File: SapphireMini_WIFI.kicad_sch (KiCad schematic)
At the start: 8 parts, among them M701 AdafruitWINC1500

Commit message: Start of layout
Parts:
- removed L701: 10uH, SapphineMinimal:NR3012T100M, symbol Device:L
- added C601: 22uF, Capacitor_SMD:C_0805_2012Metric, symbol Device:C
- C701: footprint Capacitor_SMD:C_0603_1608Metric -> Capacitor_SMD:C_0805_2012Metric; Voltage (none) -> 16
- C702: footprint Capacitor_SMD:C_0603_1608Metric -> Capacitor_SMD:C_0402_1005Metric; Voltage (none) -> 25
- R701: value 0R25 -> 0; MPN CRCW060347R0FKEAC -> RMCF0603ZT0R00
- R702, R703: MPN (none) -> CRCW060347R0FKEAC
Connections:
- net GND: now also C601.2
- net P3V3: now also C701.1, FB701.1, C601.1
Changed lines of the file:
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@@
   (junction (at 154.94 45.72) (diameter 0) (color 0 0 0 0)
+  )
+  (junction (at 114.3 45.72) (diameter 0) (color 0 0 0 0)
   )
   (junction (at 149.86 45.72) (diameter 0) (color 0 0 0 0)
@@
     (stroke (width 0) (type default) (color 0 0 0 0))
   )
+  (wire (pts (xy 114.3 53.34) (xy 114.3 54.61))
+    (stroke (width 0) (type default) (color 0 0 0 0))
+  )
   (wire (pts (xy 160.02 45.72) (xy 154.94 45.72))
     (stroke (width 0) (type default) (color 0 0 0 0))
   )
+  (wire (pts (xy 114.3 45.72) (xy 125.73 45.72))
+    (stroke (width 0) (type default) (color 0 0 0 0))
+  )
   (wire (pts (xy 158.75 54.61) (xy 157.48 53.34))
     (stroke (width 0) (type default) (color 0 0 0 0))
   )
-  (wire (pts (xy 111.76 45.72) (xy 101.6 45.72))
-    (stroke (width 0) (type default) (color 0 0 0 0))
-  )
   (wire (pts (xy 151.13 76.2) (xy 134.62 76.2))
     (stroke (width 0) (type default) (color 0 0 0 0))
@@
     (stroke (width 0) (type default) (color 0 0 0 0))
   )
-  (wire (pts (xy 125.73 45.72) (xy 119.38 45.72))
+  (wire (pts (xy 101.6 45.72) (xy 114.3 45.72))
     (stroke (width 0) (type default) (color 0 0 0 0))
   )
@@
     (property "Reference" "C702" (id 0) (at 146.05 46.99 0))
     (property "Value" "100nF" (id 1) (at 146.05 52.07 0))
-    (property "Footprint" "Capacitor_SMD:C_0603_1608Metric" (id 2) (at 150.8252 53.34 0)
+    (property "Footprint" "Capacitor_SMD:C_0402_1005Metric" (id 2) (at 150.8252 53.34 0)
       (effects (font (size 1.27 1.27)) hide)
     )
@@
     )
     (property "Populate" "1" (id 7) (at 149.86 49.53 0)
+      (effects (font (size 1.27 1.27)) hide)
+    )
+    (property "Voltage" "25" (id 8) (at 149.86 49.53 0)
       (effects (font (size 1.27 1.27)) hide)
     )
@@
     (property "Reference" "C701" (id 0) (at 121.92 46.99 0))
     (property "Value" "22uF" (id 1) (at 123.19 52.07 0))
-    (property "Footprint" "Capacitor_SMD:C_0603_1608Metric" (id 2) (at 126.6952 53.34 0)
+    (property "Footprint" "Capacitor_SMD:C_0805_2012Metric" (id 2) (at 126.6952 53.34 0)
       (effects (font (size 1.27 1.27)) hide)
     )
@@
     )
     (property "Populate" "1" (id 7) (at 125.73 49.53 0)
+      (effects (font (size 1.27 1.27)) hide)
+    )
+    (property "Voltage" "16" (id 8) (at 125.73 49.53 0)
       (effects (font (size 1.27 1.27)) hide)
     )
@@
     (in_bom yes) (on_board yes)
     (property "Reference" "R701" (id 0) (at 140.97 40.64 90))
-    (property "Value" "0R25" (id 1) (at 140.97 43.18 90))
+    (property "Value" "0" (id 1) (at 140.97 43.18 90))
     (property "Footprint" "Resistor_SMD:R_0603_1608Metric" (id 2) (at 140.97 45.72 0)
       (effects (font (size 1.27 1.27)) hide)
@@
       (effects (font (size 1.27 1.27)) hide)
     )
-    (property "MPN" "CRCW060347R0FKEAC" (id 7) (at 140.97 45.72 0)
+    (property "MPN" "RMCF0603ZT0R00" (id 7) (at 140.97 45.72 0)
       (effects (font (size 1.27 1.27)) hide)
     )
@@
       (effects (font (size 1.27 1.27)) hide)
     )
-    (property "Description" "47 Ohms ±1% 0.1W, 1/10W Chip Resistor 0603" (id 13) (at 140.97 45.72 0)
+    (property "Description" "0 Ohms Jumper 0.1W, 1/10W Chip Resistor 0603 (1608 Metric) Automotive AEC-Q200 Thick Film" (id 13) (at 140.97 45.72 0)
       (effects (font (size 1.27 1.27)) hide)
     )
@@
       (effects (font (size 1.27 1.27)) hide)
     )
+    (property "Description" "47 Ohms ±1% 0.1W, 1/10W Chip Resistor 0603" (id 4) (at 154.94 76.2 0)
+      (effects (font (size 1.27 1.27)) hide)
+    )
+    (property "MPN" "CRCW060347R0FKEAC" (id 5) (at 154.94 76.2 0)
+      (effects (font (size 1.27 1.27)) hide)
+    )
     (pin "1")
     (pin "2")
@@
     )
     (property "Datasheet" "~" (id 3) (at 154.94 71.12 0)
+      (effects (font (size 1.27 1.27)) hide)
+    )
+    (property "Description" "47 Ohms ±1% 0.1W, 1/10W Chip Resistor 0603" (id 4) (at 154.94 71.12 0)
+      (effects (font (size 1.27 1.27)) hide)
+    )
+    (property "MPN" "CRCW060347R0FKEAC" (id 5) (at 154.94 71.12 0)
+      (effects (font (size 1.27 1.27)) hide)
+    )
+    (pin "1")
+    (pin "2")
+  )
+  (symbol (lib_id "power:GND") (at 114.3 54.61 0) (unit 1)
+    (in_bom yes) (on_board yes)
+    (property "Reference" "#PWR0108" (id 0) (at 114.3 60.96 0)
+      (effects (font (size 1.27 1.27)) hide)
+    )
+    (property "Value" "GND" (id 1) (at 114.427 59.0042 0))
+    (property "Footprint" "" (id 2) (at 114.3 54.61 0)
+      (effects (font (size 1.27 1.27)) hide)
+    )
+    (property "Datasheet" "" (id 3) (at 114.3 54.61 0)
+      (effects (font (size 1.27 1.27)) hide)
+    )
+    (pin "1")
+  )
+  (symbol (lib_id "Device:C") (at 114.3 49.53 0) (unit 1)
+    (in_bom yes) (on_board yes)
+    (property "Reference" "C601" (id 0) (at 110.49 46.99 0))
+    (property "Value" "22uF" (id 1) (at 111.76 52.07 0))
+    (property "Footprint" "Capacitor_SMD:C_0805_2012Metric" (id 2) (at 115.2652 53.34 0)
+      (effects (font (size 1.27 1.27)) hide)
+    )
+    (property "Datasheet" "~" (id 3) (at 114.3 49.53 0)
+      (effects (font (size 1.27 1.27)) hide)
+    )
+    (property "Description" "22 µF ±20% 25V Ceramic Capacitor X5R 0805 (2012 Metric)" (id 4) (at 114.3 49.53 0)
+      (effects (font (size 1.27 1.27)) hide)
+    )
+    (property "MPN" "CL21A226MAYNNNE" (id 5) (at 114.3 49.53 0)
+      (effects (font (size 1.27 1.27)) hide)
+    )
+    (property "Manufacturer" "Samsung" (id 6) (at 114.3 49.53 0)
+      (effects (font (size 1.27 1.27)) hide)
+    )
+    (property "Populate" "1" (id 7) (at 114.3 49.53 0)
+      (effects (font (size 1.27 1.27)) hide)
+    )
+    (property "Voltage" "16" (id 8) (at 114.3 49.53 0)
       (effects (font (size 1.27 1.27)) hide)
     )
@@
       (effects (font (size 1.27 1.27)) hide)
     )
-    (pin "1")
-    (pin "2")
-  )
-  (symbol (lib_id "Device:L") (at 115.57 45.72 90) (unit 1)
-    (in_bom yes) (on_board yes)
-    (property "Reference" "L701" (id 0) (at 114.3 44.45 90)
-      (effects (font (size 1.27 1.27)) (justify left))
-    )
-    (property "Value" "10uH" (id 1) (at 120.65 44.45 90)
-      (effects (font (size 1.27 1.27)) (justify left))
-    )
-    (property "Footprint" "SapphineMinimal:NR3012T100M" (id 2) (at 115.57 45.72 0)
-      (effects (font (size 1.27 1.27)) hide)
-    )
-    (property "Datasheet" "~" (id 3) (at 115.57 45.72 0)
-      (effects (font (size 1.27 1.27)) hide)
-    )
-    (property "Description" "FIXED IND 10UH 630MA 348MOHM SMD" (id 4) (at 115.57 45.72 0)
-      (effects (font (size 1.27 1.27)) hide)
-    )
-    (property "MPN" "NR3012T100M" (id 5) (at 115.57 45.72 0)
-      (effects (font (size 1.27 1.27)) hide)
-    )
-    (property "Manufacturer" "Taiyo Yuden" (id 6) (at 115.57 45.72 0)
-      (effects (font (size 1.27 1.27)) hide)
-    )

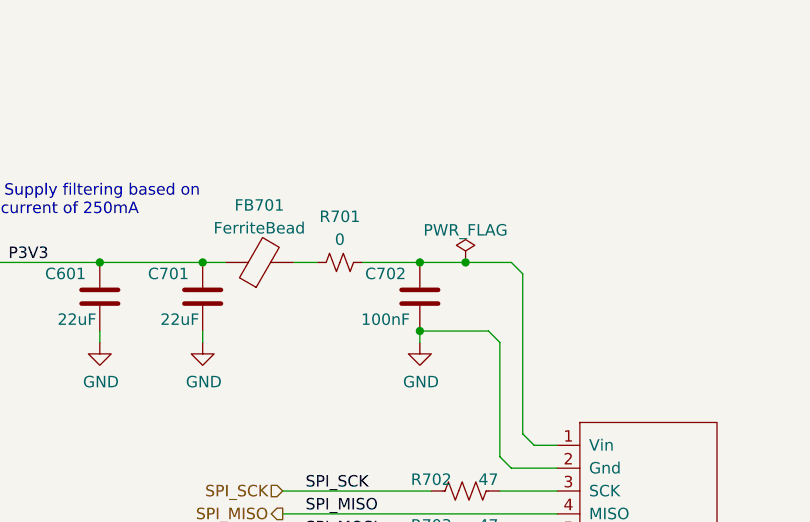
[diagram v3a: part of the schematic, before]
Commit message: updated new layout - no routing
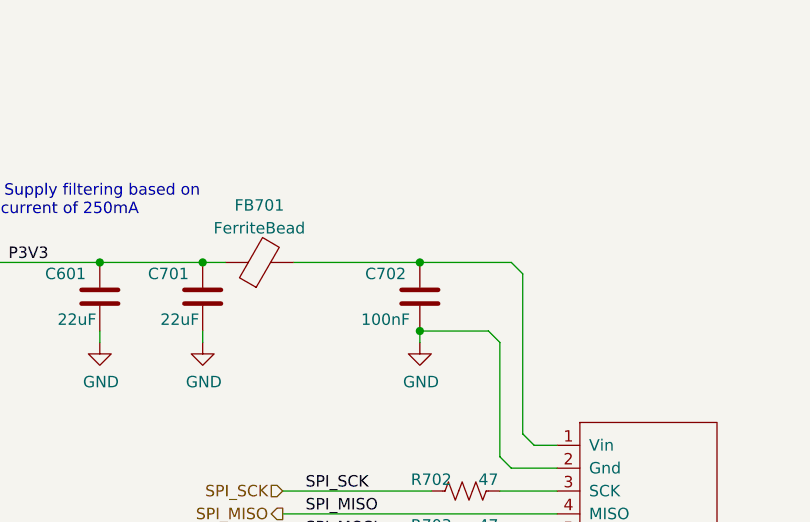
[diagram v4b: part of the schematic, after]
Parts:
- removed R701: 0, Resistor_SMD:R_0603_1608Metric, symbol Device:R_Small_US
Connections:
- net at C702.1, M701.1 (Vin): now also FB701.2
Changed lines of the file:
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@@
     (comment 2 "Markup copy w/ errors!")
-  )
-  (junction (at 154.94 45.72) (diameter 0) (color 0 0 0 0)
   )
   (junction (at 114.3 45.72) (diameter 0) (color 0 0 0 0)
@@
     (stroke (width 0) (type default) (color 0 0 0 0))
   )
+  (wire (pts (xy 135.89 45.72) (xy 149.86 45.72))
+    (stroke (width 0) (type default) (color 0 0 0 0))
+  )
   (wire (pts (xy 162.56 66.04) (xy 161.29 64.77))
     (stroke (width 0) (type default) (color 0 0 0 0))
@@
     (stroke (width 0) (type default) (color 0 0 0 0))
   )
-  (wire (pts (xy 135.89 45.72) (xy 138.43 45.72))
-    (stroke (width 0) (type default) (color 0 0 0 0))
-  )
-  (wire (pts (xy 154.94 45.72) (xy 149.86 45.72))
+  (wire (pts (xy 149.86 45.72) (xy 160.02 45.72))
     (stroke (width 0) (type default) (color 0 0 0 0))
   )
@@
     (stroke (width 0) (type default) (color 0 0 0 0))
   )
-  (wire (pts (xy 160.02 45.72) (xy 154.94 45.72))
-    (stroke (width 0) (type default) (color 0 0 0 0))
-  )
   (wire (pts (xy 114.3 45.72) (xy 125.73 45.72))
     (stroke (width 0) (type default) (color 0 0 0 0))
@@
   )
   (wire (pts (xy 165.1 78.74) (xy 134.62 78.74))
-    (stroke (width 0) (type default) (color 0 0 0 0))
-  )
-  (wire (pts (xy 143.51 45.72) (xy 149.86 45.72))
     (stroke (width 0) (type default) (color 0 0 0 0))
   )
@@
     (pin "1")
   )
-  (symbol (lib_id "Device:R_Small_US") (at 140.97 45.72 90) (unit 1)
-    (in_bom yes) (on_board yes)
-    (property "Reference" "R701" (id 0) (at 140.97 40.64 90))
-    (property "Value" "0" (id 1) (at 140.97 43.18 90))
-    (property "Footprint" "Resistor_SMD:R_0603_1608Metric" (id 2) (at 140.97 45.72 0)
-      (effects (font (size 1.27 1.27)) hide)
-    )
-    (property "Datasheet" "~" (id 3) (at 140.97 45.72 0)
-      (effects (font (size 1.27 1.27)) hide)
-    )
-    (property "DigiKey Price" "0.05" (id 4) (at 140.97 45.72 0)
-      (effects (font (size 1.27 1.27)) hide)
-    )
-    (property "Manufacturer" "Vishay" (id 5) (at 140.97 45.72 0)
-      (effects (font (size 1.27 1.27)) hide)
-    )
-    (property "Tolerance" "5%" (id 6) (at 140.97 45.72 0)
-      (effects (font (size 1.27 1.27)) hide)
-    )
-    (property "MPN" "RMCF0603ZT0R00" (id 7) (at 140.97 45.72 0)
-      (effects (font (size 1.27 1.27)) hide)
-    )
-    (property "Populate" "1" (id 8) (at 140.97 45.72 0)
-      (effects (font (size 1.27 1.27)) hide)
-    )
-    (property "MacroFab_PN" "MF-RES-0603-47" (id 9) (at 140.97 45.72 0)
-      (effects (font (size 1.27 1.27)) hide)
-    )
-    (property "Digi-Key_PN" "541-5440-1-ND" (id 10) (at 140.97 45.72 0)
-      (effects (font (size 1.27 1.27)) hide)
-    )
-    (property "Distributor" "Digikey" (id 11) (at 140.97 45.72 0)
-      (effects (font (size 1.27 1.27)) hide)
-    )
-    (property "DPN" "541-5440-1-ND" (id 12) (at 140.97 45.72 0)
-      (effects (font (size 1.27 1.27)) hide)
-    )
-    (property "Description" "0 Ohms Jumper 0.1W, 1/10W Chip Resistor 0603 (1608 Metric) Automotive AEC-Q200 Thick Film" (id 13) (at 140.97 45.72 0)
-      (effects (font (size 1.27 1.27)) hide)
-    )
-    (pin "1")
-    (pin "2")
-  )
   (symbol (lib_id "Device:R_US") (at 154.94 76.2 270) (unit 1)
     (in_bom yes) (on_board yes)
@@
     (pin "2")
   )
-  (symbol (lib_id "power:PWR_FLAG") (at 154.94 45.72 0) (unit 1)
-    (in_bom yes) (on_board yes) (fields_autoplaced)
-    (property "Reference" "#FLG0701" (id 0) (at 154.94 43.815 0)
-      (effects (font (size 1.27 1.27)) hide)
-    )
-    (property "Value" "PWR_FLAG" (id 1) (at 154.94 42.1442 0))
-    (property "Footprint" "" (id 2) (at 154.94 45.72 0)
-      (effects (font (size 1.27 1.27)) hide)
-    )
-    (property "Datasheet" "~" (id 3) (at 154.94 45.72 0)
-      (effects (font (size 1.27 1.27)) hide)
-    )
-    (pin "1")
-  )
 )

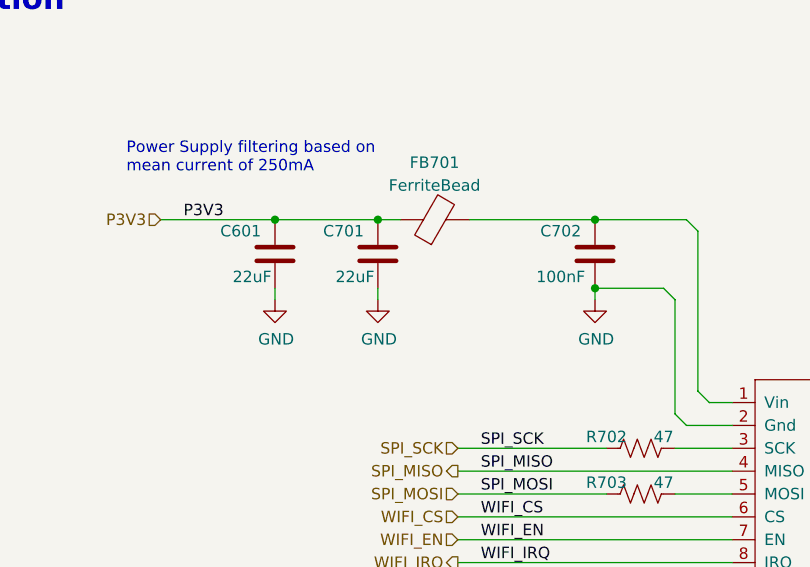
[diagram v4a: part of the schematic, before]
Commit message: 6 Layer Routing
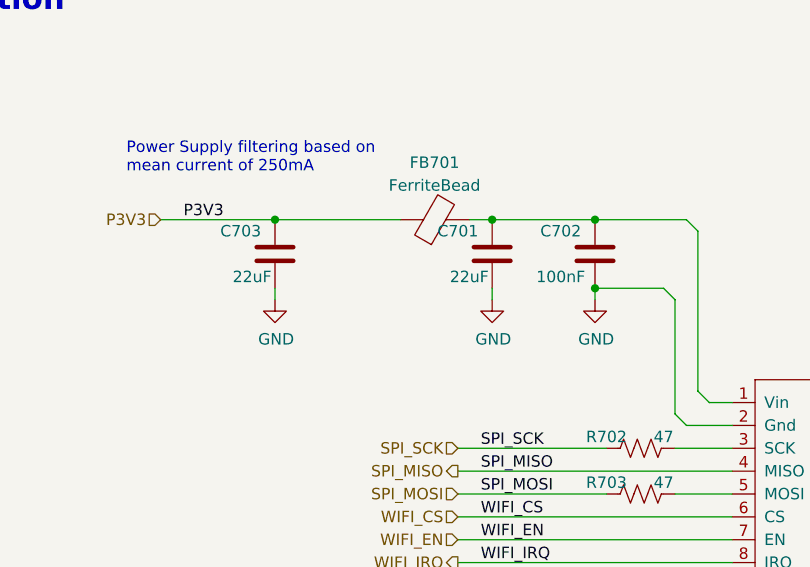
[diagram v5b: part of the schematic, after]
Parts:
- FB701: footprint Inductor_SMD:L_0201_0603Metric -> Inductor_SMD:L_0603_1608Metric
- renumbered C601 to C703
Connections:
- net P3V3: no longer C701.1
- net at C702.1, FB701.2, M701.1 (Vin): now also C701.1
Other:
- moved on the sheet: C701
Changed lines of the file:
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@@
     (comment 2 "Markup copy w/ errors!")
   )
+  (junction (at 138.43 45.72) (diameter 0) (color 0 0 0 0)
+  )
   (junction (at 114.3 45.72) (diameter 0) (color 0 0 0 0)
   )
   (junction (at 149.86 45.72) (diameter 0) (color 0 0 0 0)
-  )
-  (junction (at 125.73 45.72) (diameter 0) (color 0 0 0 0)
   )
   (junction (at 149.86 53.34) (diameter 0) (color 0 0 0 0)
@@
     (stroke (width 0) (type default) (color 0 0 0 0))
   )
-  (wire (pts (xy 135.89 45.72) (xy 149.86 45.72))
+  (wire (pts (xy 135.89 45.72) (xy 138.43 45.72))
+    (stroke (width 0) (type default) (color 0 0 0 0))
+  )
+  (wire (pts (xy 138.43 45.72) (xy 149.86 45.72))
     (stroke (width 0) (type default) (color 0 0 0 0))
   )
@@
     (stroke (width 0) (type default) (color 0 0 0 0))
   )
-  (wire (pts (xy 125.73 54.61) (xy 125.73 53.34))
+  (wire (pts (xy 138.43 54.61) (xy 138.43 53.34))
     (stroke (width 0) (type default) (color 0 0 0 0))
   )
@@
     (stroke (width 0) (type default) (color 0 0 0 0))
   )
-  (wire (pts (xy 114.3 45.72) (xy 125.73 45.72))
-    (stroke (width 0) (type default) (color 0 0 0 0))
-  )
   (wire (pts (xy 158.75 54.61) (xy 157.48 53.34))
     (stroke (width 0) (type default) (color 0 0 0 0))
@@
     (stroke (width 0) (type default) (color 0 0 0 0))
   )
-  (wire (pts (xy 128.27 45.72) (xy 125.73 45.72))
+  (wire (pts (xy 114.3 45.72) (xy 128.27 45.72))
     (stroke (width 0) (type default) (color 0 0 0 0))
   )
@@
     (pin "2")
   )
-  (symbol (lib_id "Device:C") (at 125.73 49.53 0) (unit 1)
-    (in_bom yes) (on_board yes)
-    (property "Reference" "C701" (id 0) (at 121.92 46.99 0))
-    (property "Value" "22uF" (id 1) (at 123.19 52.07 0))
-    (property "Footprint" "Capacitor_SMD:C_0805_2012Metric" (id 2) (at 126.6952 53.34 0)
-      (effects (font (size 1.27 1.27)) hide)
-    )
-    (property "Datasheet" "~" (id 3) (at 125.73 49.53 0)
-      (effects (font (size 1.27 1.27)) hide)
-    )
-    (property "Description" "22 µF ±20% 25V Ceramic Capacitor X5R 0805 (2012 Metric)" (id 4) (at 125.73 49.53 0)
-      (effects (font (size 1.27 1.27)) hide)
-    )
-    (property "MPN" "CL21A226MAYNNNE" (id 5) (at 125.73 49.53 0)
-      (effects (font (size 1.27 1.27)) hide)
-    )
-    (property "Manufacturer" "Samsung" (id 6) (at 125.73 49.53 0)
-      (effects (font (size 1.27 1.27)) hide)
-    )
-    (property "Populate" "1" (id 7) (at 125.73 49.53 0)
-      (effects (font (size 1.27 1.27)) hide)
-    )
-    (property "Voltage" "16" (id 8) (at 125.73 49.53 0)
-      (effects (font (size 1.27 1.27)) hide)
-    )
-    (pin "1")
-    (pin "2")
-  )
-  (symbol (lib_id "power:GND") (at 125.73 54.61 0) (unit 1)
-    (in_bom yes) (on_board yes)
-    (property "Reference" "#PWR0701" (id 0) (at 125.73 60.96 0)
-      (effects (font (size 1.27 1.27)) hide)
-    )
-    (property "Value" "GND" (id 1) (at 125.857 59.0042 0))
-    (property "Footprint" "" (id 2) (at 125.73 54.61 0)
-      (effects (font (size 1.27 1.27)) hide)
-    )
-    (property "Datasheet" "" (id 3) (at 125.73 54.61 0)
+  (symbol (lib_id "Device:C") (at 138.43 49.53 0) (unit 1)
+    (in_bom yes) (on_board yes)
+    (property "Reference" "C701" (id 0) (at 134.62 46.99 0))
+    (property "Value" "22uF" (id 1) (at 135.89 52.07 0))
+    (property "Footprint" "Capacitor_SMD:C_0805_2012Metric" (id 2) (at 139.3952 53.34 0)
+      (effects (font (size 1.27 1.27)) hide)
+    )
+    (property "Datasheet" "~" (id 3) (at 138.43 49.53 0)
+      (effects (font (size 1.27 1.27)) hide)
+    )
+    (property "Description" "22 µF ±20% 25V Ceramic Capacitor X5R 0805 (2012 Metric)" (id 4) (at 138.43 49.53 0)
+      (effects (font (size 1.27 1.27)) hide)
+    )
+    (property "MPN" "CL21A226MAYNNNE" (id 5) (at 138.43 49.53 0)
+      (effects (font (size 1.27 1.27)) hide)
+    )
+    (property "Manufacturer" "Samsung" (id 6) (at 138.43 49.53 0)
+      (effects (font (size 1.27 1.27)) hide)
+    )
+    (property "Populate" "1" (id 7) (at 138.43 49.53 0)
+      (effects (font (size 1.27 1.27)) hide)
+    )
+    (property "Voltage" "16" (id 8) (at 138.43 49.53 0)
+      (effects (font (size 1.27 1.27)) hide)
+    )
+    (pin "1")
+    (pin "2")
+  )
+  (symbol (lib_id "power:GND") (at 138.43 54.61 0) (unit 1)
+    (in_bom yes) (on_board yes)
+    (property "Reference" "#PWR0701" (id 0) (at 138.43 60.96 0)
+      (effects (font (size 1.27 1.27)) hide)
+    )
+    (property "Value" "GND" (id 1) (at 138.557 59.0042 0))
+    (property "Footprint" "" (id 2) (at 138.43 54.61 0)
+      (effects (font (size 1.27 1.27)) hide)
+    )
+    (property "Datasheet" "" (id 3) (at 138.43 54.61 0)
       (effects (font (size 1.27 1.27)) hide)
     )
@@
   (symbol (lib_id "Device:C") (at 114.3 49.53 0) (unit 1)
     (in_bom yes) (on_board yes)
-    (property "Reference" "C601" (id 0) (at 110.49 46.99 0))
+    (property "Reference" "C703" (id 0) (at 110.49 46.99 0))
     (property "Value" "22uF" (id 1) (at 111.76 52.07 0))
     (property "Footprint" "Capacitor_SMD:C_0805_2012Metric" (id 2) (at 115.2652 53.34 0)
@@
     (property "Reference" "FB701" (id 0) (at 132.0292 39.3786 90))
     (property "Value" "FerriteBead" (id 1) (at 132.0292 41.9155 90))
-    (property "Footprint" "Inductor_SMD:L_0201_0603Metric" (id 2) (at 132.08 47.498 90)
-      (effects (font (size 1.27 1.27)) hide)
-    )
+    (property "Footprint" "Inductor_SMD:L_0603_1608Metric" (id 2) (at 132.08 47.498 90)
+      (effects (font (size 1.27 1.27)) hide)
+    )

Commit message: Added optional RSCK footprint
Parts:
- C701, C703: Attrition (none) -> 0
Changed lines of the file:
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@@
+      (effects (font (size 1.27 1.27)) hide)
+    )
+    (property "Attrition" "0" (id 9) (at 138.43 49.53 0)
       (effects (font (size 1.27 1.27)) hide)
     )
@@
       (effects (font (size 1.27 1.27)) hide)
     )
+    (property "Attrition" "0" (id 9) (at 114.3 49.53 0)
+      (effects (font (size 1.27 1.27)) hide)
+    )

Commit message: Release to OSH Park
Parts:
- added R601, R602: 0, Resistor_SMD:R_0603_1608Metric, symbol Device:R_Small_US
- added R603, R604: 47, Resistor_SMD:R_0603_1608Metric, symbol Device:R_US
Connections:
- net SPI_MISO: now also R602.1; no longer M701.4 (MISO)
- net WSPI_SCK: now reaches M701.3 (SCK), R702.1
- net WSPI_SCK: now also R604.1
- net WSPI_MOSI: now reaches M701.5 (MOSI), R703.1
- net WSPI_MOSI: now also R603.1
- new net SPI2_MISO: R601.1
- new net SPI2_MOSI: R603.2
- new net SPI2_SCK: R604.2
- new net WSPI_MISO: M701.4 (MISO), R601.2, R602.2
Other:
- moved on the sheet: R702, R703
